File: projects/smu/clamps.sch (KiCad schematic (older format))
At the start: 36 parts, among them P401 CONN_01X12, U401 DAC8734, U402 LM324, U404 LM324

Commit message: fix dg444 and dac power inputs
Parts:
- removed C407, C408, C409, C410, C411, C412: C, Capacitors_SMD:C_1206, symbol C
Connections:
- no-connect marks 27 -> 29
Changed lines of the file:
@@
 Wire Wire Line
 	12700 5700 12300 5700
-$Comp
-L C C407
-U 1 1 58623221
-P 3600 7100
-F 0 "C407" H 3625 7200 50  0000 L CNN
-F 1 "C" H 3625 7000 50  0000 L CNN
-F 2 "Capacitors_SMD:C_1206" H 3638 6950 50  0001 C CNN
-F 3 "" H 3600 7100 50  0000 C CNN
-	1    3600 7100
-	1    0    0    -1
-$EndComp
-$Comp
-L C C411
-U 1 1 58623228
-P 4100 7100
-F 0 "C411" H 4125 7200 50  0000 L CNN
-F 1 "C" H 4125 7000 50  0000 L CNN
-F 2 "Capacitors_SMD:C_1206" H 4138 6950 50  0001 C CNN
-F 3 "" H 4100 7100 50  0000 C CNN
-	1    4100 7100
-	1    0    0    -1
-$EndComp
 Connection ~ 3600 6950
-Text GLabel 3600 7250 3    60   Input ~ 0
-AGND
-$Comp
-L C C409
-U 1 1 58623231
-P 3850 7100
-F 0 "C409" H 3875 7200 50  0000 L CNN
-F 1 "C" H 3875 7000 50  0000 L CNN
-F 2 "Capacitors_SMD:C_1206" H 3888 6950 50  0001 C CNN
-F 3 "" H 3850 7100 50  0000 C CNN
-	1    3850 7100
-	1    0    0    -1
-$EndComp
 Connection ~ 3850 6950
-Text GLabel 3850 7250 3    60   Input ~ 0
-AGND
 Connection ~ 4100 6950
-Text GLabel 4100 7250 3    60   Input ~ 0
-AGND
-$Comp
-L C C408
-U 1 1 5862323C
-P 3600 8100
-F 0 "C408" H 3625 8200 50  0000 L CNN
-F 1 "C" H 3625 8000 50  0000 L CNN
-F 2 "Capacitors_SMD:C_1206" H 3638 7950 50  0001 C CNN
-F 3 "" H 3600 8100 50  0000 C CNN
-	1    3600 8100
-	1    0    0    -1
-$EndComp
-$Comp
-L C C412
-U 1 1 58623243
-P 4100 8100
-F 0 "C412" H 4125 8200 50  0000 L CNN
-F 1 "C" H 4125 8000 50  0000 L CNN
-F 2 "Capacitors_SMD:C_1206" H 4138 7950 50  0001 C CNN
-F 3 "" H 4100 8100 50  0000 C CNN
-	1    4100 8100
-	1    0    0    -1
-$EndComp
 Connection ~ 3600 7950
-Text GLabel 3600 8250 3    60   Input ~ 0
-AGND
-$Comp
-L C C410
-U 1 1 5862324C
-P 3850 8100
-F 0 "C410" H 3875 8200 50  0000 L CNN
-F 1 "C" H 3875 8000 50  0000 L CNN
-F 2 "Capacitors_SMD:C_1206" H 3888 7950 50  0001 C CNN
-F 3 "" H 3850 8100 50  0000 C CNN
-	1    3850 8100
-	1    0    0    -1
-$EndComp
 Connection ~ 3850 7950
-Text GLabel 3850 8250 3    60   Input ~ 0
-AGND
 Connection ~ 4100 7950
-Text GLabel 4100 8250 3    60   Input ~ 0
-AGND
 Wire Wire Line
 	5350 6900 5650 6900
@@
 Wire Wire Line
 	14350 1350 14350 1550
+Text GLabel 5800 5500 0    60   Input ~ 0
+V-OUT-3
+Text GLabel 5800 5750 0    60   Input ~ 0
+V-OUT-4
+NoConn ~ 5800 5500
+NoConn ~ 5800 5750
 $EndSCHEMATC

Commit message: fixed design rules checks
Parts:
- removed P401: CONN_01X12, Pin_Headers:Pin_Header_Straight_1x12, symbol CONN_01X12
- added P401: CONN_01X24, symbol CONN_01X24
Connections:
- net labels added: DAC_CS, DAC_LDAC, DAC_RST, DAC_SDI, DAC_SDO, DAC_SLCK
- wire segments 128 -> 145
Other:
- moved on the sheet: U402A, U402B
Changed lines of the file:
@@
 $Descr A3 16535 11693
 encoding utf-8
-Sheet 4 4
+Sheet 3 3
 Title ""
 Date ""
@@
 	2650 6850 2650 6950
 Wire Wire Line
-	2650 6950 4350 6950
+	2650 6950 3600 6950
 Connection ~ 2850 6950
 Text GLabel 2850 7250 3    60   Input ~ 0
@@
 	2650 7850 2650 7950
 Wire Wire Line
-	2650 7950 4350 7950
+	2650 7950 3600 7950
 Connection ~ 2850 7950
 Text GLabel 2850 8250 3    60   Input ~ 0
@@
 OUT
 NoConn ~ 5650 7400
-NoConn ~ 5650 7550
-NoConn ~ 5650 7500
 NoConn ~ 11550 4700
 NoConn ~ 11650 4700
@@
 Text GLabel 5350 7300 0    60   Input ~ 0
 V-FB
-$Comp
-L CONN_01X12 P401
-U 1 1 58623218
-P 5850 7050
-F 0 "P401" H 5850 7700 50  0000 C CNN
-F 1 "CONN_01X12" V 5950 7050 50  0000 C CNN
-F 2 "Pin_Headers:Pin_Header_Straight_1x12" H 5850 7050 50  0001 C CNN
-F 3 "" H 5850 7050 50  0000 C CNN
-	1    5850 7050
-	1    0    0    -1
-$EndComp
 Wire Wire Line
 	12700 5700 12300 5700
 Connection ~ 3600 6950
-Connection ~ 3850 6950
-Connection ~ 4100 6950
 Connection ~ 3600 7950
-Connection ~ 3850 7950
-Connection ~ 4100 7950
 Wire Wire Line
 	5350 6900 5650 6900
 Wire Wire Line
 	5650 7300 5350 7300
-NoConn ~ 5650 7600
 Wire Wire Line
 	10600 1500 10400 1500
@@
 L LM324 U402
 U 2 1 58A7EF6E
-P 9200 7250
-F 0 "U402" H 9200 7450 50  0000 L CNN
-F 1 "LM324" H 9200 7050 50  0000 L CNN
-F 2 "" H 9150 7350 50  0000 C CNN
-F 3 "" H 9250 7450 50  0000 C CNN
-	2    9200 7250
+P 10050 7250
+F 0 "U402" H 10050 7450 50  0000 L CNN
+F 1 "LM324" H 10050 7050 50  0000 L CNN
+F 2 "" H 10000 7350 50  0000 C CNN
+F 3 "" H 10100 7450 50  0000 C CNN
+	2    10050 7250
 	1    0    0    -1
 $EndComp
@@
 L LM324 U402
 U 1 1 58A7EFD7
-P 8250 7250
-F 0 "U402" H 8250 7450 50  0000 L CNN
-F 1 "LM324" H 8250 7050 50  0000 L CNN
-F 2 "" H 8200 7350 50  0000 C CNN
-F 3 "" H 8300 7450 50  0000 C CNN
-	1    8250 7250
-	1    0    0    -1
-$EndComp
-Wire Wire Line
-	7950 7150 7950 7800
-Wire Wire Line
-	8900 7800 8900 7150
-Text GLabel 7800 7800 0    60   Input ~ 0
-AGND
-Connection ~ 8900 7350
-Connection ~ 7950 7350
-Connection ~ 7950 7800
-Wire Wire Line
-	7800 7800 8900 7800
-NoConn ~ 9500 7250
-NoConn ~ 8550 7250
+P 9100 7250
+F 0 "U402" H 9100 7450 50  0000 L CNN
+F 1 "LM324" H 9100 7050 50  0000 L CNN
+F 2 "" H 9050 7350 50  0000 C CNN
+F 3 "" H 9150 7450 50  0000 C CNN
+	1    9100 7250
+	1    0    0    -1
+$EndComp
+Wire Wire Line
+	8800 7150 8800 7800
+Wire Wire Line
+	9750 7800 9750 7150
+Text GLabel 8650 7800 0    60   Input ~ 0
+AGND
+Connection ~ 9750 7350
+Connection ~ 8800 7350
+Connection ~ 8800 7800
+Wire Wire Line
+	8650 7800 9750 7800
+NoConn ~ 10350 7250
+NoConn ~ 9400 7250
 $Comp
 L LM324 U404
@@
 Text GLabel 9150 2700 1    60   Input ~ 0
 +VE
-Text GLabel 13750 1550 3    60   Input ~ 0
+Text GLabel 5250 5650 3    60   Input ~ 0
 +VE
 $Comp
 L PWR_FLAG #FLG01
 U 1 1 58AA88D7
-P 13750 1350
-F 0 "#FLG01" H 13750 1445 50  0001 C CNN
-F 1 "PWR_FLAG" H 13750 1530 50  0000 C CNN
-F 2 "" H 13750 1350 50  0000 C CNN
-F 3 "" H 13750 1350 50  0000 C CNN
-	1    13750 1350
-	1    0    0    -1
-$EndComp
-Wire Wire Line
-	13750 1350 13750 1550
+P 5250 5450
+F 0 "#FLG01" H 5250 5545 50  0001 C CNN
+F 1 "PWR_FLAG" H 5250 5630 50  0000 C CNN
+F 2 "" H 5250 5450 50  0000 C CNN
+F 3 "" H 5250 5450 50  0000 C CNN
+	1    5250 5450
+	1    0    0    -1
+$EndComp
+Wire Wire Line
+	5250 5450 5250 5650
 $Comp
 L PWR_FLAG #FLG02
 U 1 1 58AAC503
-P 14350 1350
-F 0 "#FLG02" H 14350 1445 50  0001 C CNN
-F 1 "PWR_FLAG" H 14350 1530 50  0000 C CNN
-F 2 "" H 14350 1350 50  0000 C CNN
-F 3 "" H 14350 1350 50  0000 C CNN
-	1    14350 1350
-	1    0    0    -1
-$EndComp
-Text GLabel 14350 1550 3    60   Input ~ 0
+P 5850 5450
+F 0 "#FLG02" H 5850 5545 50  0001 C CNN
+F 1 "PWR_FLAG" H 5850 5630 50  0000 C CNN
+F 2 "" H 5850 5450 50  0000 C CNN
+F 3 "" H 5850 5450 50  0000 C CNN
+	1    5850 5450
+	1    0    0    -1
+$EndComp
+Text GLabel 5850 5650 3    60   Input ~ 0
 -VE
 Wire Wire Line
-	14350 1350 14350 1550
-Text GLabel 5800 5500 0    60   Input ~ 0
+	5850 5450 5850 5650
+Text GLabel 5350 8400 0    60   Input ~ 0
 V-OUT-3
-Text GLabel 5800 5750 0    60   Input ~ 0
+Text GLabel 5350 8500 0    60   Input ~ 0
 V-OUT-4
-NoConn ~ 5800 5500
-NoConn ~ 5800 5750
+Text GLabel 5350 7500 0    60   Input ~ 0
+DAC_CS
+Text GLabel 5350 7600 0    60   Input ~ 0
+DAC_SLCK
+Text GLabel 5350 7700 0    60   Input ~ 0
+DAC_SDI
+Text GLabel 5350 7800 0    60   Input ~ 0
+DAC_SDO
+Text GLabel 5350 7900 0    60   Input ~ 0
+DAC_LDAC
+Text GLabel 5350 8000 0    60   Input ~ 0
+DAC_RST
+$Comp
+L CONN_01X24 P401
+U 1 1 58ACF484
+P 5850 7650
+F 0 "P401" H 5850 8900 50  0000 C CNN
+F 1 "CONN_01X24" V 5950 7650 50  0000 C CNN
+F 2 "" H 5850 7650 50  0000 C CNN
+F 3 "" H 5850 7650 50  0000 C CNN
+	1    5850 7650
+	1    0    0    -1
+$EndComp
+Wire Wire Line
+	5350 7500 5650 7500
+Wire Wire Line
+	5350 7600 5650 7600
+Wire Wire Line
+	5350 7700 5650 7700
+Wire Wire Line
+	5350 7800 5650 7800
+Wire Wire Line
+	5350 7900 5650 7900
+Wire Wire Line
+	5350 8000 5650 8000
+Text GLabel 2550 2100 0    60   Input ~ 0
+DAC_CS
+Text GLabel 2550 2200 0    60   Input ~ 0
+DAC_SLCK
+Text GLabel 2550 2300 0    60   Input ~ 0
+DAC_SDI
+Text GLabel 2550 2400 0    60   Input ~ 0
+DAC_SDO
+Text GLabel 2550 2500 0    60   Input ~ 0
+DAC_LDAC
+Text GLabel 2550 2600 0    60   Input ~ 0
+DAC_RST
+Wire Wire Line
+	2550 2100 3250 2100
+Wire Wire Line
+	2550 2200 3250 2200
+Wire Wire Line
+	2550 2300 3250 2300
+Wire Wire Line
+	2550 2400 3250 2400
+Wire Wire Line
+	2550 2500 3250 2500
+Wire Wire Line
+	2550 2600 3250 2600
+Text GLabel 3850 5550 0    60   Input ~ 0
+AGND
+Text GLabel 3850 5650 0    60   Input ~ 0
+DGND
+Text GLabel 3850 5750 0    60   Input ~ 0
+REFGND
+Wire Wire Line
+	3850 5550 3850 5750
+Wire Wire Line
+	5350 8200 5650 8200
+Wire Wire Line
+	5350 8300 5650 8300
+Text GLabel 5350 8200 0    60   Input ~ 0
+V-SET
+Text GLabel 5350 8300 0    60   Input ~ 0
+I-SET
+Wire Wire Line
+	5350 8400 5650 8400
+Wire Wire Line
+	5350 8500 5650 8500
+NoConn ~ 5650 7100
+NoConn ~ 5650 8100
+NoConn ~ 5650 8600
+NoConn ~ 5650 8700
+NoConn ~ 5650 8800
 $EndSCHEMATC

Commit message: add analog switch
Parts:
- removed P401: CONN_01X24, symbol CONN_01X24
- added C407, C408: C, Capacitors_SMD:C_1206, symbol C
- added P401: CONN_01X34, symbol CONN_01X34
- added U405: DG444, Housings_SOIC:SOIC-16_3.9x9.9mm_Pitch1.27mm, symbol DG444
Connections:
- net labels added: REF_IN1, REF_IN2, REF_IN3, REF_IN4
- net labels removed: REF-CTL
- wire segments 145 -> 169
- no-connect marks 29 -> 35
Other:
- moved on the sheet: C401, C402, C403, C404, C405, C406, R401, R402, R403, U401, U402A, U402B

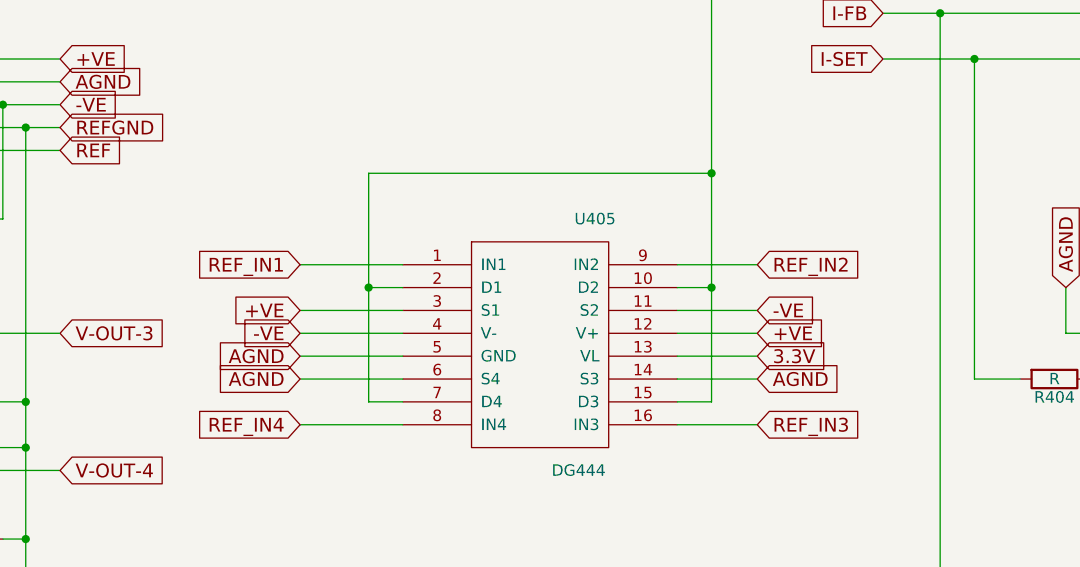
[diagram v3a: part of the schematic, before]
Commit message: add net-ties where needed
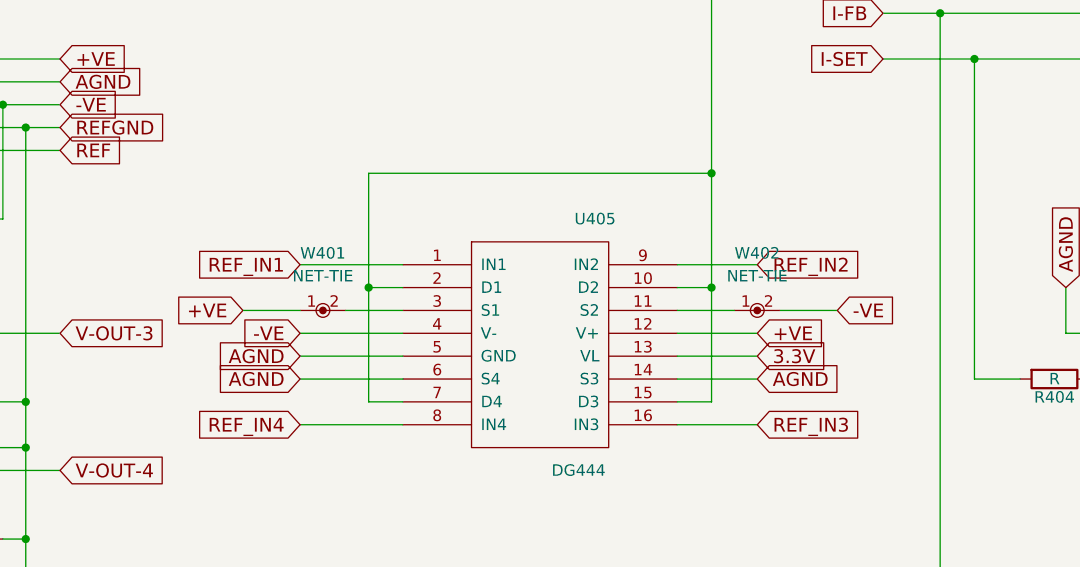
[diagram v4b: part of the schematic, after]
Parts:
- added W401, W402: NET-TIE, conn-test:NET-TIE, symbol NET-TIE
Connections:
- net +VE: now also W401.1; no longer U405.3 (S1)
- net -VE: now also W402.2; no longer U405.11 (S2)
- new net: U405.11 (S2), W402.1
- new net: U405.3 (S1), W401.2
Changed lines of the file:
@@
 	5650 3200 5800 3200
-Wire Wire Line
-	7000 2800 7350 2800
 Wire Wire Line
 	5650 2200 5650 3200
@@
 	7150 2200 5650 2200
 Connection ~ 7150 2200
-Text GLabel 5350 2800 0    60   Input ~ 0
+Text GLabel 5100 2800 0    60   Input ~ 0
 +VE
-Wire Wire Line
-	5350 2800 5800 2800
-Text GLabel 7350 2800 2    60   Input ~ 0
+Text GLabel 7700 2800 2    60   Input ~ 0
 -VE
 Wire Wire Line
@@
 Wire Wire Line
 	5350 6450 5650 6450
+Wire Wire Line
+	5800 2800 5550 2800
+Wire Wire Line
+	5100 2800 5350 2800
+$Comp
+L NET-TIE W402
+U 1 1 58A83D51
+P 7350 2800
+F 0 "W402" H 7350 3050 50  0000 C CNN
+F 1 "NET-TIE" H 7350 2950 50  0000 C CNN
+F 2 "conn-test:NET-TIE" H 7350 2700 50  0001 C CNN
+F 3 "" H 7350 2800 60  0000 C CNN
+	1    7350 2800
+	1    0    0    -1
+$EndComp
+Wire Wire Line
+	7700 2800 7450 2800
+Wire Wire Line
+	7250 2800 7000 2800
+$Comp
+L NET-TIE W401
+U 1 1 58A8468B
+P 5450 2800
+F 0 "W401" H 5450 3050 50  0000 C CNN
+F 1 "NET-TIE" H 5450 2950 50  0000 C CNN
+F 2 "conn-test:NET-TIE" H 5450 2700 50  0001 C CNN
+F 3 "" H 5450 2800 60  0000 C CNN
+	1    5450 2800
+	1    0    0    -1
+$EndComp
 $EndSCHEMATC
